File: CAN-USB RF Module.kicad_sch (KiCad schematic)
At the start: 15 parts, among them IC1 ESDALC6V1W5, J1 Conn_01x06_Pin, SW1 RESET, SW2 BOOT0, U1 STM32L442KCU6

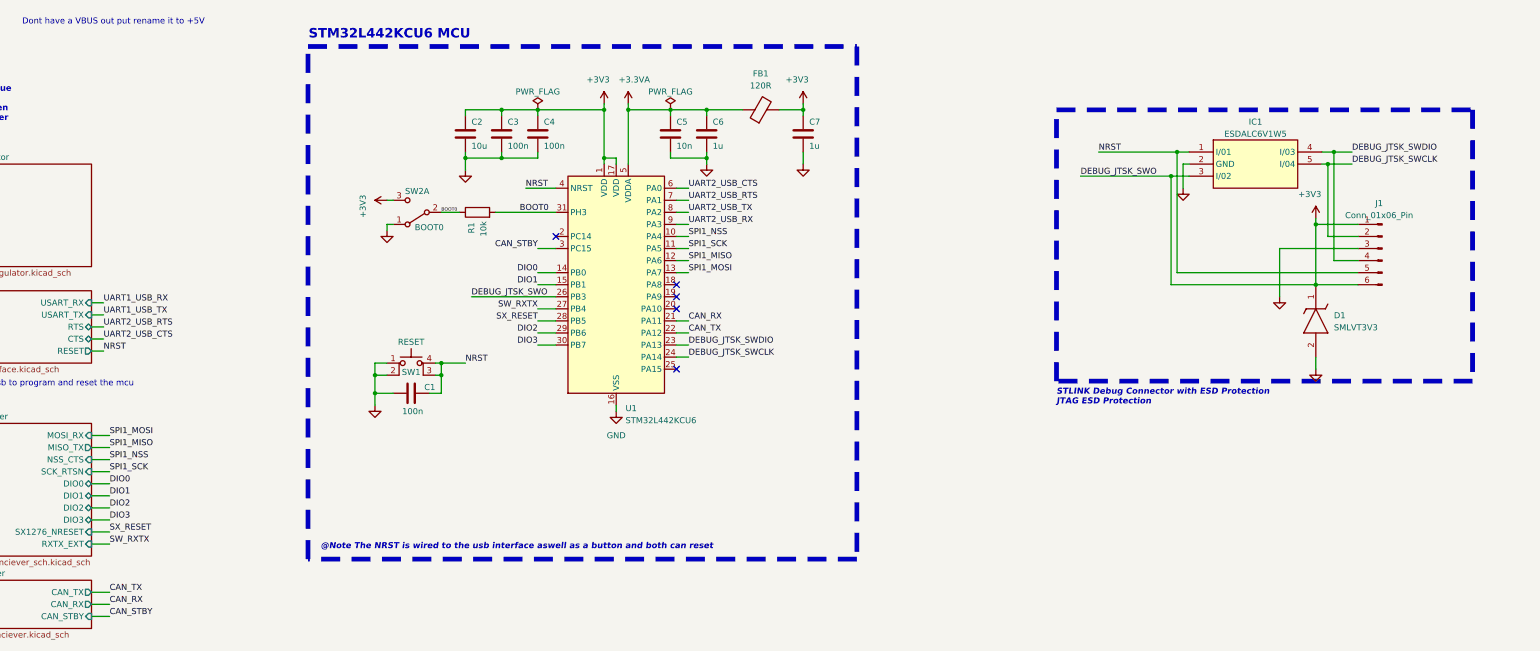
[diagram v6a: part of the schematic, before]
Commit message: Added all schmatics about to change LDO 1 to buck
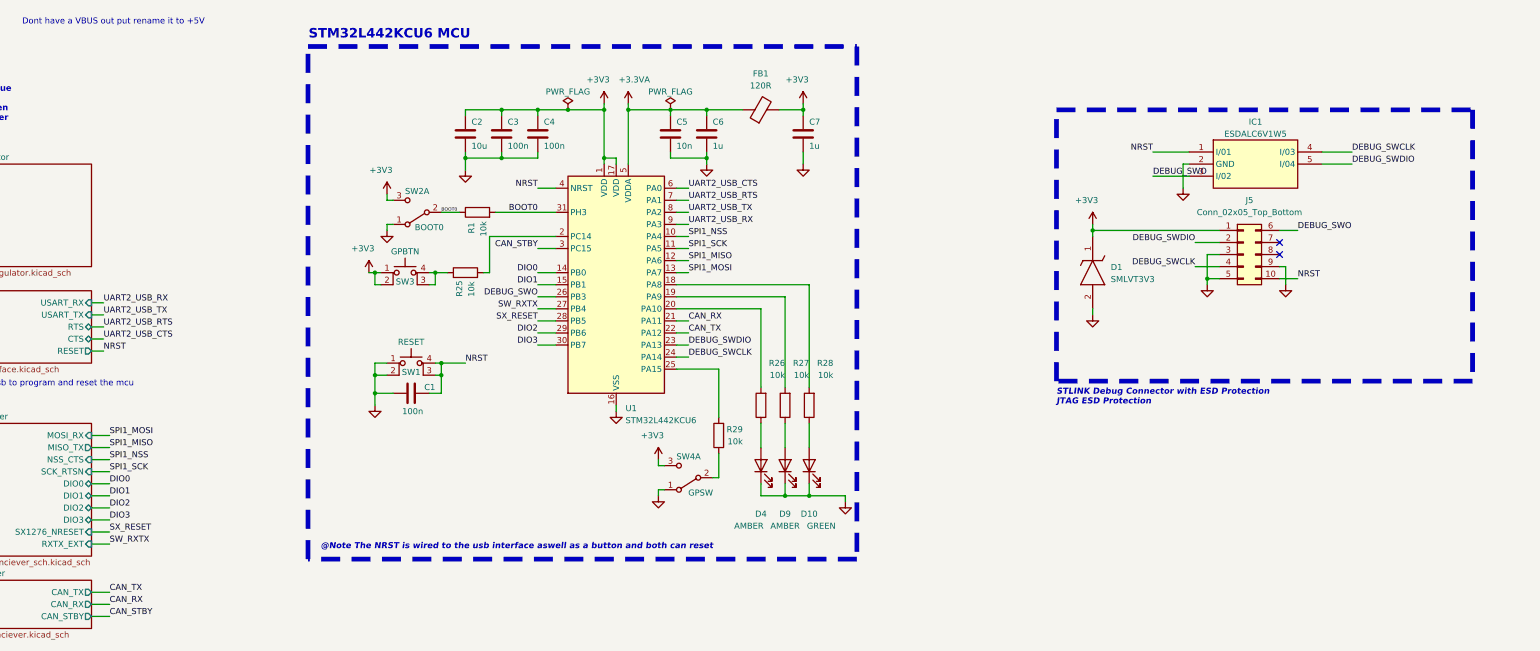
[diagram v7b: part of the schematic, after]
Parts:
- removed J1: Conn_01x06_Pin, Connector_PinHeader_2.54mm:PinHeader_1x06_P2.54mm_Vertical, symbol Connector:Conn_01x06_Pin
- added D10: GREEN, LED_SMD:LED_0603_1608Metric, symbol Device:LED
- added D4, D9: AMBER, LED_SMD:LED_0603_1608Metric, symbol Device:LED
- added J5: Conn_02x05_Top_Bottom, Connector_PinHeader_2.54mm:PinHeader_2x05_P2.54mm_Vertical, symbol Connector_Generic:Conn_02x05_Top_Bottom
- added R25, R29: 10k, Resistor_SMD:R_0402_1005Metric, symbol Device:R
- added R26, R27, R28: 10k, Resistor_SMD:R_0603_1608Metric, symbol Device:R
- added SW3: GPBTN, footprints:SMD_025816_WRE, symbol Switch:SW_MEC_5E
- added SW4: GPSW, Button_Switch_SMD:SW_SPDT_PCM12, symbol Switch:SW_DPDT_x2
- C6: footprint Capacitor_SMD:C_0603_1608Metric -> Capacitor_SMD:C_0402_1005Metric
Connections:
- net +3V3: now also J5.1 (Pin_1), SW3.1, SW3.2, SW4.3 (C); no longer IC1.3 (I/02), U1.26 (PB3)
- net GND: now also D10.1 (K), D4.1 (K), D9.1 (K), J5.3 (Pin_3), J5.5 (Pin_5), J5.9 (Pin_9), SW4.1 (A)
- net NRST: now also J5.10 (Pin_10)
- net at U1.18 (PA8): now also R28.2
- net at U1.19 (PA9): now also R27.2
- net at U1.2 (PC14): now also R25.2
- net at U1.20 (PA10): now also R26.2
- net at U1.25 (PA15): now also R29.2
- net DEBUG_JTSK_SWCLK renamed DEBUG_SWCLK
- net DEBUG_SWCLK: now also IC1.4 (I/03), J5.4 (Pin_4); no longer IC1.5 (I/04)
- net DEBUG_JTSK_SWDIO renamed DEBUG_SWDIO
- net DEBUG_SWDIO: now also IC1.5 (I/04), J5.2 (Pin_2); no longer IC1.4 (I/03)
- new net: R29.1, SW4.2 (B)
- new net: D9.2 (A), R27.1
- new net: R25.1, SW3.3 (K), SW3.4 (A)
- new net: D4.2 (A), R28.1
- new net: D10.2 (A), R26.1
- new net DEBUG_SWO: IC1.3 (I/02), J5.6 (Pin_6), U1.26 (PB3)
- no-connect marks 5 -> 2
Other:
- moved on the sheet: D1

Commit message: Done design
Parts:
- R25, R29, SW3, SW4: now not fitted; now left out of the parts list
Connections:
- net at R25.2: no longer U1.2 (PC14)
- net at R29.2: no longer U1.25 (PA15)
- new net DIO4: U1.25 (PA15)
- new net DIO5: U1.2 (PC14)
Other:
- sheet LoRa Tranciever ports: added DIO4, DIO5; removed none
- note added: "@Application Note I am using a JLC PCB impedence controlled stack up. JLC04161H-7628 Stackup"
